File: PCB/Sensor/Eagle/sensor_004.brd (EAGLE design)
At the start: 142.8 x 97.5 mm, 254 parts, among them IC1 LMV324, IC10 LMV324, IC11 LMV324, IC12 LMV324, IC13 LMV324, IC14 LMV324, IC15 LMV324, IC16 LMV324, IC17 LMV324, IC18 LMV324, IC19 LMV324, IC2 LMV324, IC20 LMV324, IC21 LMV324, IC22 LMV324, IC23 LMV324, IC24 LMV324, IC3 LMV324, IC4 LMV324, IC5 LMV324, IC6 LMV324, IC7 LMV324, IC8 LMV324, IC9 LMV324, U1 74HC4067, U2 74HC4067, U3 74HC4067, U4 74HC4067, U5 74HC4067, U6 74HC4067

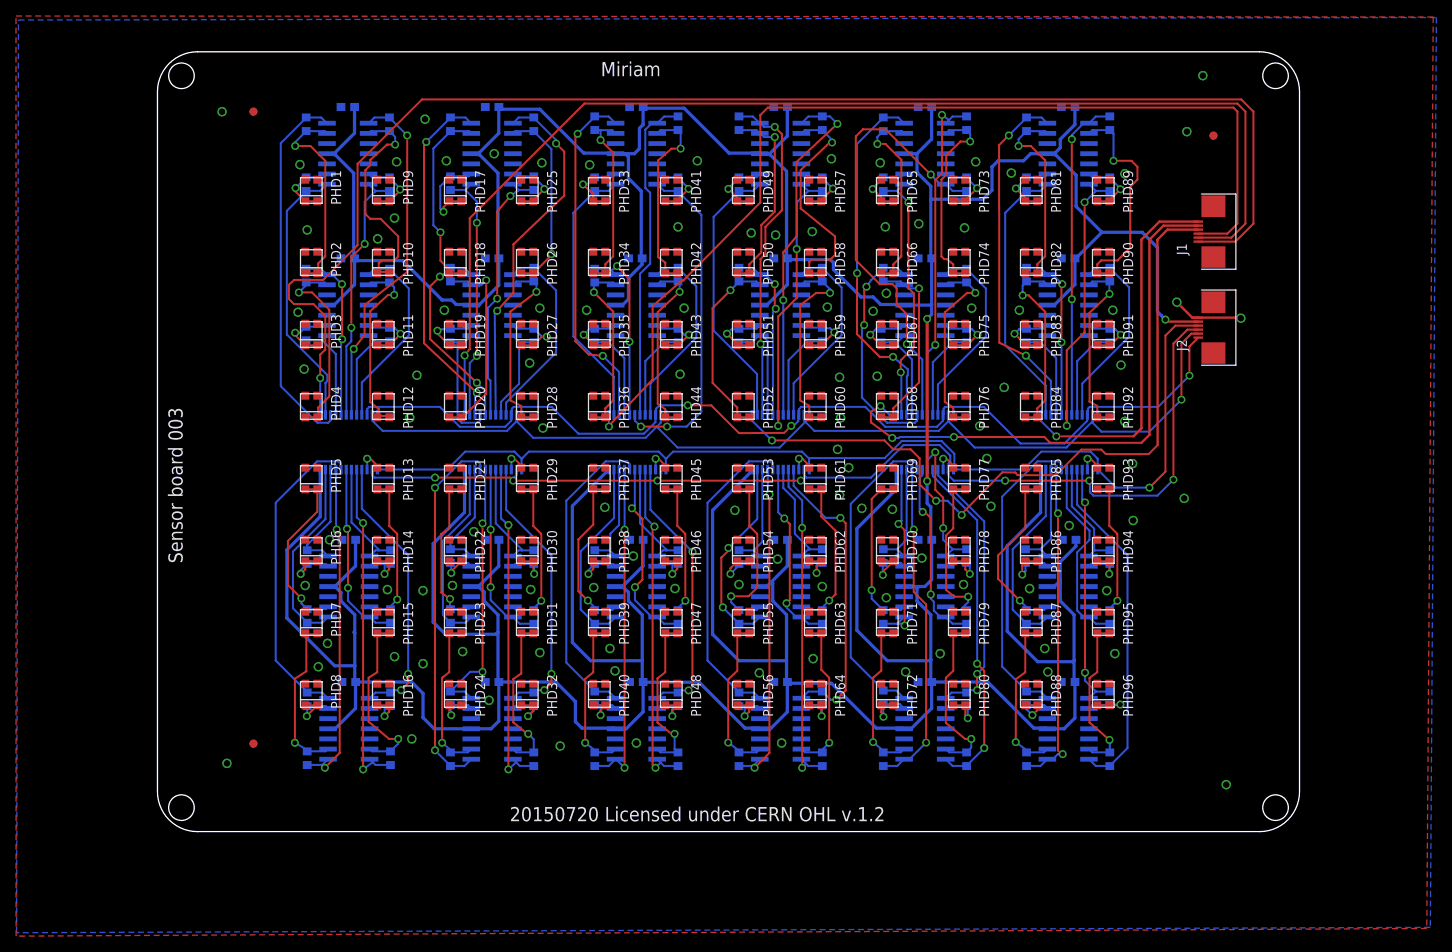
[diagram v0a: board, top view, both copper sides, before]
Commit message: change sensor board and case
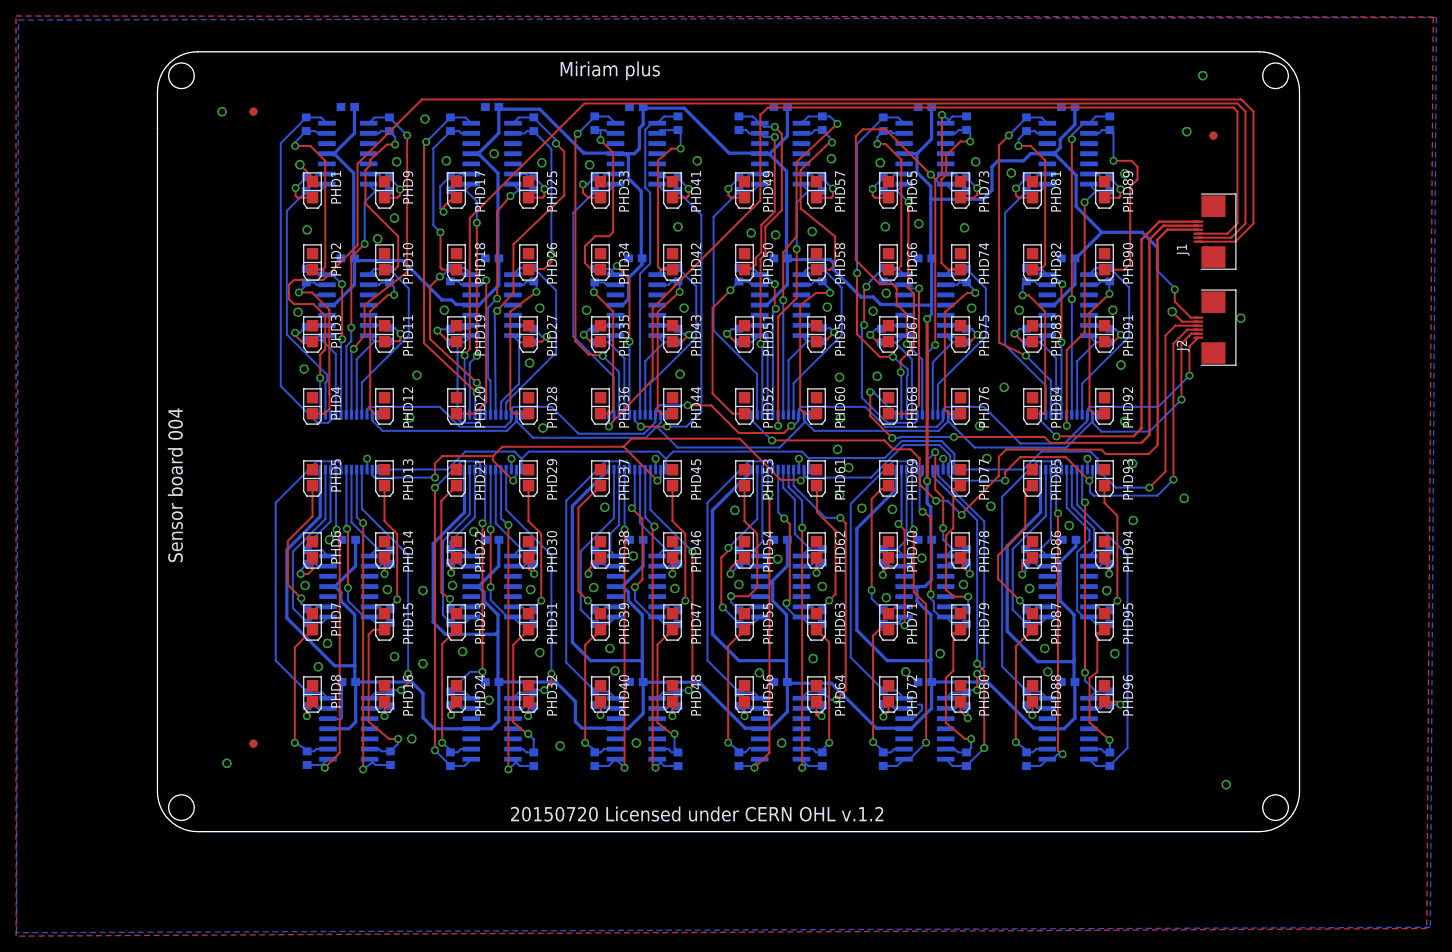
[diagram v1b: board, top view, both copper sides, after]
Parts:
- PHD1, PHD10, PHD11, PHD12, PHD13, PHD14, PHD15, PHD16, PHD17, PHD18, PHD19, PHD2, PHD20, PHD21, PHD22, PHD23, PHD24, PHD25, PHD26, PHD27, PHD28, PHD29, PHD3, PHD30, PHD31, PHD32, PHD33, PHD34, PHD35, PHD36, PHD37, PHD38, PHD39, PHD4, PHD40, PHD41, PHD42, PHD43, PHD44, PHD45, PHD46, PHD47, PHD48, PHD49, PHD5, PHD50, PHD51, PHD52, PHD53, PHD54, PHD55, PHD56, PHD57, PHD58, PHD59, PHD6, PHD60, PHD61, PHD62, PHD63, PHD64, PHD65, PHD66, PHD67, PHD68, PHD69, PHD7, PHD70, PHD71, PHD72, PHD73, PHD74, PHD75, PHD76, PHD77, PHD78, PHD79, PHD8, PHD80, PHD81, PHD82, PHD83, PHD84, PHD85, PHD86, PHD87, PHD88, PHD89, PHD9, PHD90, PHD91, PHD92, PHD93, PHD94, PHD95, PHD96: device Miroculus:PD_0.2 -> Miroculus:PD_2
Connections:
- net +5V: now also J2.6; no longer J2.5
- net GND: now also J2.5; no longer J2.6, PHD1.2, PHD10.2, PHD11.2, PHD12.2, PHD13.2, PHD14.2, PHD15.2, PHD16.2, PHD17.2, PHD18.2, PHD19.2, PHD2.2, PHD20.2, PHD21.2, PHD22.2, PHD23.2, PHD24.2, PHD25.2, PHD26.2, PHD27.2, PHD28.2, PHD29.2, PHD3.2, PHD30.2, PHD31.2, PHD32.2, PHD33.2, PHD34.2, PHD35.2, PHD36.2, PHD37.2, PHD38.2, PHD39.2, PHD4.2, PHD40.2, PHD41.2, PHD42.2, PHD43.2, PHD44.2, PHD45.2, PHD46.2, PHD47.2, PHD48.2, PHD49.2, PHD5.2, PHD50.2, PHD51.2, PHD52.2, PHD53.2, PHD54.2, PHD55.2, PHD56.2, PHD57.2, PHD58.2, PHD59.2, PHD6.2, PHD60.2, PHD61.2, PHD62.2, PHD63.2, PHD64.2, PHD65.2, PHD66.2, PHD67.2, PHD68.2, PHD69.2, PHD7.2, PHD70.2, PHD71.2, PHD72.2, PHD73.2, PHD74.2, PHD75.2, PHD76.2, PHD77.2, PHD78.2, PHD79.2, PHD8.2, PHD80.2, PHD81.2, PHD82.2, PHD83.2, PHD84.2, PHD85.2, PHD86.2, PHD87.2, PHD88.2, PHD89.2, PHD9.2, PHD90.2, PHD91.2, PHD92.2, PHD93.2, PHD94.2, PHD95.2, PHD96.2
- net PD1: now also PHD1.2; no longer PHD1.3, PHD1.4
- net PD10: now also PHD10.2; no longer PHD10.3, PHD10.4
- net PD11: now also PHD11.2; no longer PHD11.3, PHD11.4
- net PD12: now also PHD12.2; no longer PHD12.3, PHD12.4
- net PD13: now also PHD13.2; no longer PHD13.3, PHD13.4
- net PD14: now also PHD14.2; no longer PHD14.3, PHD14.4
- net PD15: now also PHD15.2; no longer PHD15.3, PHD15.4
- net PD16: now also PHD16.2; no longer PHD16.3, PHD16.4
- net PD17: now also PHD17.2; no longer PHD17.3, PHD17.4
- net PD18: now also PHD18.2; no longer PHD18.3, PHD18.4
- net PD19: now also PHD19.2; no longer PHD19.3, PHD19.4
- net PD2: now also PHD2.2; no longer PHD2.3, PHD2.4
- net PD20: now also PHD20.2; no longer PHD20.3, PHD20.4
- net PD21: now also PHD21.2; no longer PHD21.3, PHD21.4
- net PD22: now also PHD22.2; no longer PHD22.3, PHD22.4
- net PD23: now also PHD23.2; no longer PHD23.3, PHD23.4
- net PD24: now also PHD24.2; no longer PHD24.3, PHD24.4
- net PD25: now also PHD25.2; no longer PHD25.3, PHD25.4
- net PD26: now also PHD26.2; no longer PHD26.3, PHD26.4
- net PD27: now also PHD27.2; no longer PHD27.3, PHD27.4
- net PD28: now also PHD28.2; no longer PHD28.3, PHD28.4
- net PD29: now also PHD29.2; no longer PHD29.3, PHD29.4
- net PD3: now also PHD3.2; no longer PHD3.3, PHD3.4
- net PD30: now also PHD30.2; no longer PHD30.3, PHD30.4
- net PD31: now also PHD31.2; no longer PHD31.3, PHD31.4
- net PD32: now also PHD32.2; no longer PHD32.3, PHD32.4
- net PD33: now also PHD33.2; no longer PHD33.3, PHD33.4
- net PD34: now also PHD34.2; no longer PHD34.3, PHD34.4
- net PD35: now also PHD35.2; no longer PHD35.3, PHD35.4
- net PD36: now also PHD36.2; no longer PHD36.3, PHD36.4
- net PD37: now also PHD37.2; no longer PHD37.3, PHD37.4
- net PD38: now also PHD38.2; no longer PHD38.3, PHD38.4
- net PD39: now also PHD39.2; no longer PHD39.3, PHD39.4
- net PD4: now also PHD4.2; no longer PHD4.3, PHD4.4
- net PD40: now also PHD40.2; no longer PHD40.3, PHD40.4
- net PD41: now also PHD41.2; no longer PHD41.3, PHD41.4
- net PD42: now also PHD42.2; no longer PHD42.3, PHD42.4
- net PD43: now also PHD43.2; no longer PHD43.3, PHD43.4
- net PD44: now also PHD44.2; no longer PHD44.3, PHD44.4
- net PD45: now also PHD45.2; no longer PHD45.3, PHD45.4
- net PD46: now also PHD46.2; no longer PHD46.3, PHD46.4
- net PD47: now also PHD47.2; no longer PHD47.3, PHD47.4
- net PD48: now also PHD48.2; no longer PHD48.3, PHD48.4
- net PD49: now also PHD49.2; no longer PHD49.3, PHD49.4
- net PD5: now also PHD5.2; no longer PHD5.3, PHD5.4
- net PD50: now also PHD50.2; no longer PHD50.3, PHD50.4
- net PD51: now also PHD51.2; no longer PHD51.3, PHD51.4
- net PD52: now also PHD52.2; no longer PHD52.3, PHD52.4
- net PD53: now also PHD53.2; no longer PHD53.3, PHD53.4
- net PD54: now also PHD54.2; no longer PHD54.3, PHD54.4
- net PD55: now also PHD55.2; no longer PHD55.3, PHD55.4
- net PD56: now also PHD56.2; no longer PHD56.3, PHD56.4
- net PD57: now also PHD57.2; no longer PHD57.3, PHD57.4
- net PD58: now also PHD58.2; no longer PHD58.3, PHD58.4
- net PD59: now also PHD59.2; no longer PHD59.3, PHD59.4
- net PD6: now also PHD6.2; no longer PHD6.3, PHD6.4
- net PD60: now also PHD60.2; no longer PHD60.3, PHD60.4
- net PD61: now also PHD61.2; no longer PHD61.3, PHD61.4
- net PD62: now also PHD62.2; no longer PHD62.3, PHD62.4
- net PD63: now also PHD63.2; no longer PHD63.3, PHD63.4
- net PD64: now also PHD64.2; no longer PHD64.3, PHD64.4
- net PD65: now also PHD65.2; no longer PHD65.3, PHD65.4
- net PD66: now also PHD66.2; no longer PHD66.3, PHD66.4
- net PD67: now also PHD67.2; no longer PHD67.3, PHD67.4
- net PD68: now also PHD68.2; no longer PHD68.3, PHD68.4
- net PD69: now also PHD69.2; no longer PHD69.3, PHD69.4
- net PD7: now also PHD7.2; no longer PHD7.3, PHD7.4
- net PD70: now also PHD70.2; no longer PHD70.3, PHD70.4
- net PD71: now also PHD71.2; no longer PHD71.3, PHD71.4
- net PD72: now also PHD72.2; no longer PHD72.3, PHD72.4
- net PD73: now also PHD73.2; no longer PHD73.3, PHD73.4
- net PD74: now also PHD74.2; no longer PHD74.3, PHD74.4
- net PD75: now also PHD75.2; no longer PHD75.3, PHD75.4
- net PD76: now also PHD76.2; no longer PHD76.3, PHD76.4
- net PD77: now also PHD77.2; no longer PHD77.3, PHD77.4
- net PD78: now also PHD78.2; no longer PHD78.3, PHD78.4
- net PD79: now also PHD79.2; no longer PHD79.3, PHD79.4
- net PD8: now also PHD8.2; no longer PHD8.3, PHD8.4
- net PD80: now also PHD80.2; no longer PHD80.3, PHD80.4
- net PD81: now also PHD81.2; no longer PHD81.3, PHD81.4
- net PD82: now also PHD82.2; no longer PHD82.3, PHD82.4
- net PD83: now also PHD83.2; no longer PHD83.3, PHD83.4
- net PD84: now also PHD84.2; no longer PHD84.3, PHD84.4
- net PD85: now also PHD85.2; no longer PHD85.3, PHD85.4
- net PD86: now also PHD86.2; no longer PHD86.3, PHD86.4
- net PD87: now also PHD87.2; no longer PHD87.3, PHD87.4
- net PD88: now also PHD88.2; no longer PHD88.3, PHD88.4
- net PD89: now also PHD89.2; no longer PHD89.3, PHD89.4
- net PD9: now also PHD9.2; no longer PHD9.3, PHD9.4
- net PD90: now also PHD90.2; no longer PHD90.3, PHD90.4
- net PD91: now also PHD91.2; no longer PHD91.3, PHD91.4
- net PD92: now also PHD92.2; no longer PHD92.3, PHD92.4
- net PD93: now also PHD93.2; no longer PHD93.3, PHD93.4
- net PD94: now also PHD94.2; no longer PHD94.3, PHD94.4
- net PD95: now also PHD95.2; no longer PHD95.3, PHD95.4
- net PD96: now also PHD96.2; no longer PHD96.3, PHD96.4
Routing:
- net S2: track 135.5 -> 153.7 mm
- net PD88: track 10.1 -> 6.03 mm
- net +5V: track 784.4 -> 780.9 mm
- net PD10: track 28.8 -> 25.7 mm
- net AR4: track 72.6 -> 75.5 mm
- net PD58: track 29.3 -> 26.6 mm
- net PD90: track 28.2 -> 26.1 mm
- net PD34: track 23.2 -> 24.8 mm
- net PD77: track 23.1 -> 21.6 mm
- net PD22: track 7.75 -> 6.26 mm
- net PD40: track 7.18 -> 5.72 mm
- net PD56: track 7.08 -> 5.68 mm
- net PD70: track 8.09 -> 6.76 mm
- net PD48: track 7.10 -> 5.80 mm
- net PD46: track 7.32 -> 6.02 mm
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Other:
- board text added: "Miriam plus"
- board text added: "Sensor board 004"
- board text removed: "Miriam"
- board text removed: "Sensor board 003"
